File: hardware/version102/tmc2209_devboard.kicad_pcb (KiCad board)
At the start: 2 copper layers, 69 x 53.8 mm, 41 parts, among them J1 Conn_01x02_Male, J2 Conn_01x03_Pin, J4 motor_conn, J5 motor_conn, J6 motor_conn, SW1 SW_Push, U1 TMC2209-LA

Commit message: fixed order files and added images
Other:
- board text added: "TMC2209 devboard v1.2 github.com/neumi"
- board text removed: "TMC2209 devboard v1.0 github.com/neumi"

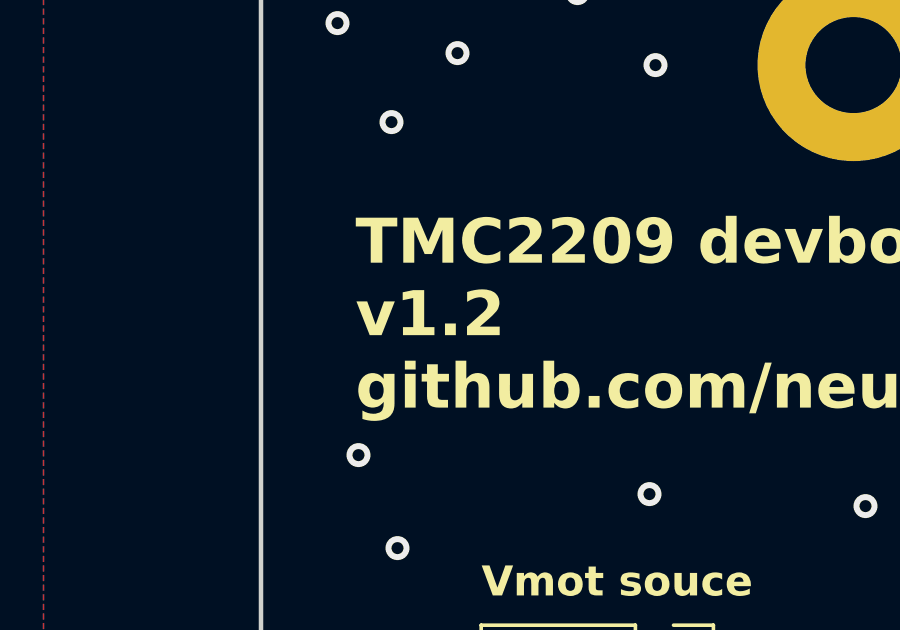
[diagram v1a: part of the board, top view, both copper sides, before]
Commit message: minor changed for version 1.3. Changed component number for JLC parts for R3 (was wrong) relates #3
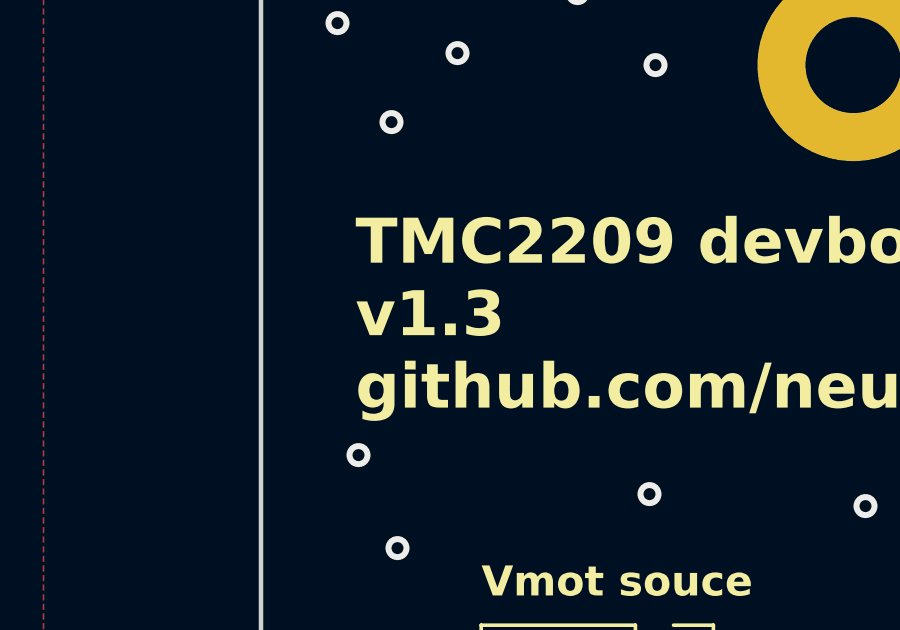
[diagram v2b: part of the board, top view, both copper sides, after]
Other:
- board text added: "TMC2209 devboard v1.3 github.com/neumi"
- board text removed: "TMC2209 devboard v1.2 github.com/neumi"
